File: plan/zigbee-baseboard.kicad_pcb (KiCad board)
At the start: 4 copper layers, 15.3 x 20.6 mm, 55 parts, among them J1 Debug_SWD_Pogo_2x3_P2.00mm, J2 EFR32MG24_Core_Expansion_L12, SW1 EVPBB2A9B000, U1 EFR32MG24B020F1536IM48-B, Y1 XTL501250-S315-038

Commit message: Adapt board size
The castellated pads currently doesn't really fit on the board.
The clearance to the lower board edge is not enough.
Therefore the board size has to get increased minimal to a size of 16x21mm
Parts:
- moved J2 0.40 mm to (133.8, 86.6)
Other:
- board size 15.3 x 20.6 mm -> 16 x 21 mm
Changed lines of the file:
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@@
 	)
 	(footprint "Smarthome:Module_EFR32MG24_Core_Castellated_L_12Pin_P2.54mm"
-		(locked yes)
 		(layer "F.Cu")
-		(at 134.2 86.64)
+		(at 133.8 86.64)
 		(property "Reference" "J2"
 			(at 5.5 0 0)
@@
 			(type default)
 		)
-		(layer "Edge.Cuts")
+		(layer "Dwgs.User")
 	)
 	(gr_line
@@
 			(type default)
 		)
-		(layer "Edge.Cuts")
+		(layer "Dwgs.User")
 	)
 	(gr_line
@@
 			(type default)
 		)
-		(layer "Edge.Cuts")
+		(layer "Dwgs.User")
 	)
 	(gr_line
@@
 			(type default)
 		)
+		(layer "Dwgs.User")
+	)
+	(gr_rect
+		(start 133.5 82)
+		(end 149.5 103)
+		(stroke
+			(width 0.05)
+			(type default)
+		)
+		(fill no)
 		(layer "Edge.Cuts")
 	)

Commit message: Place castellated pads on board edge
After adapting the board edges, place the castellated pads again on the board edge.
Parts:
- moved J2 0.50 mm to (133.5, 86.2)
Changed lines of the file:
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@@
 	)
 	(footprint "Smarthome:Module_EFR32MG24_Core_Castellated_L_12Pin_P2.54mm"
+		(locked yes)
 		(layer "F.Cu")
-		(at 133.8 86.64)
+		(at 133.5 86.24)
 		(property "Reference" "J2"
 			(at 5.5 0 0)

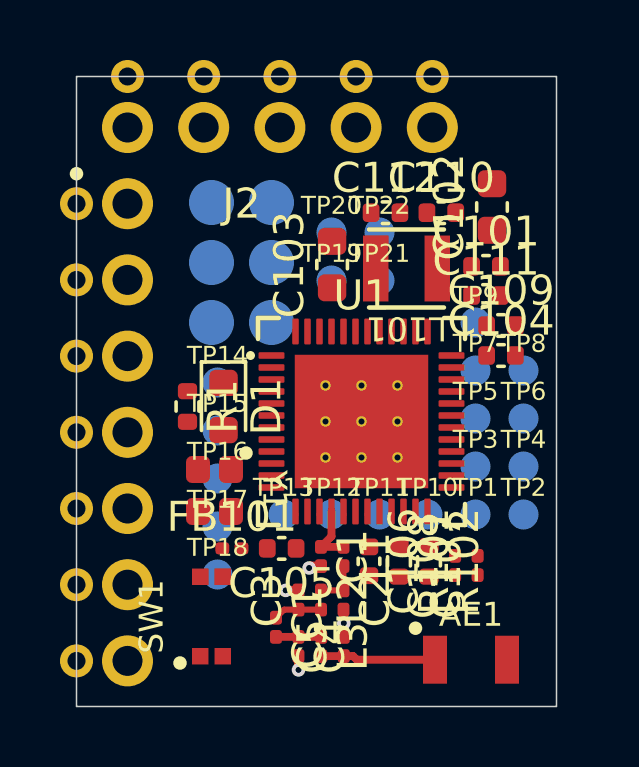
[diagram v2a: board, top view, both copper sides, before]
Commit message: Place GND area on F.Cu and In1.Cu
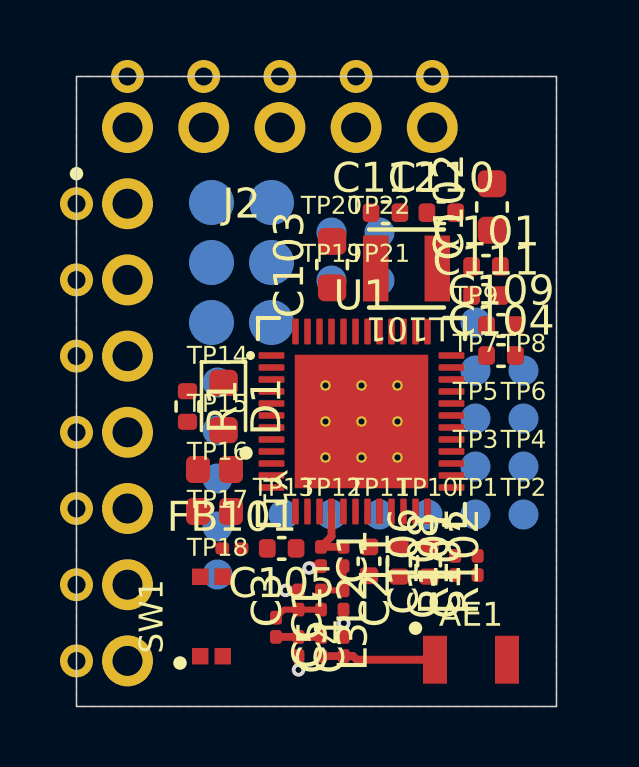
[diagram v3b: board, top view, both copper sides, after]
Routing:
- added copper zone on F.Cu, net GND
- added copper zone on In1.Cu, net GND
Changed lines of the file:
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@@
+	)
+	(zone
+		(net "GND")
+		(layer "F.Cu")
+		(hatch edge 0.5)
+		(priority 1)
+		(connect_pads yes
+			(clearance 0.2)
+		)
+		(min_thickness 0.2)
+		(fill yes
+			(thermal_gap 0.5)
+			(thermal_bridge_width 0.5)
+			(island_removal_mode 0)
+		)
+		(polygon
+			(pts
+				(xy 149.5 82) (xy 149.5 103) (xy 133.5 103) (xy 133.5 82)
+			)
+		)
 	)
 	(zone
@@
 			)
 		)
+	)
+	(zone
+		(net "GND")
+		(layer "In1.Cu")
+		(hatch edge 0.5)
+		(connect_pads yes
+			(clearance 0.2)
+		)
+		(min_thickness 0.2)
+		(fill yes
+			(thermal_gap 0.5)
+			(thermal_bridge_width 0.5)
+			(island_removal_mode 0)
+		)
+		(polygon
+			(pts
+				(xy 149.5 82) (xy 149.5 103) (xy 133.5 103) (xy 133.5 82)
+			)
+		)

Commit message: Route power lines
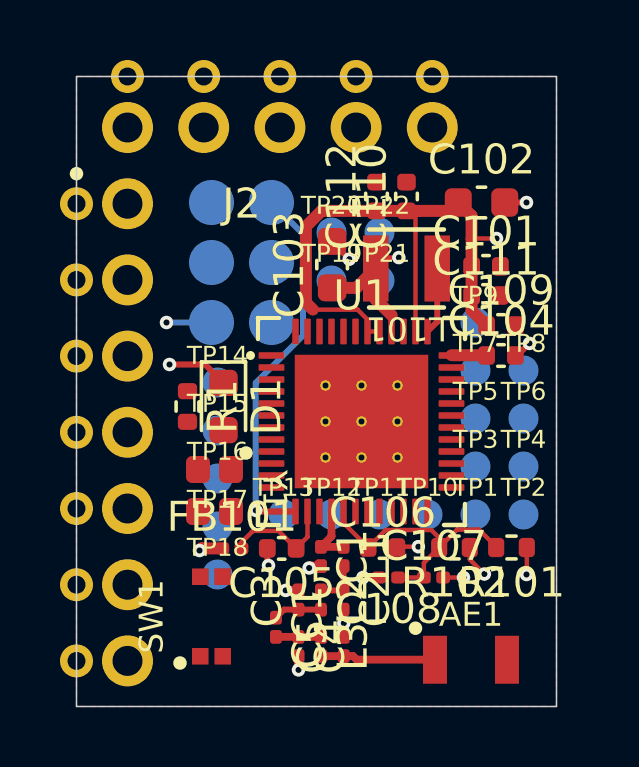
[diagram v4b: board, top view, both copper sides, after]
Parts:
- moved R101 3.78 mm to (148.0, 97.7), turned to 180 degrees
- moved C108 2.26 mm to (143.9, 98.7), turned to 180 degrees
- moved C107 1.52 mm to (145.4, 98.7), turned to 0 degrees
- moved C110 1.28 mm to (144.5, 86.0), turned to 90 degrees
- moved R102 0.97 mm to (146.1, 97.7), turned to 180 degrees
- moved C106 0.64 mm to (143.7, 97.7), turned to 0 degrees
- moved C112 0.62 mm to (143.5, 86.0), turned to 90 degrees
- moved C102 0.38 mm to (147.0, 86.2), turned to 0 degrees
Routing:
- net VBAT: track 0.00 -> 32.9 mm, vias 0 -> 2
- net VDCDC: track 0.00 -> 28.3 mm, vias 0 -> 3
- net ~{RESET}: track 0.00 -> 12.7 mm, vias 0 -> 1
- net PAVDD: track 0.00 -> 9.06 mm
- net GND: track 2.24 -> 10.6 mm, vias 4 -> 13
- net RFVDD: track 0.00 -> 3.81 mm
- net VREGSW: track 0.00 -> 2.23 mm
- net DECOUPLE: track 0.00 -> 1.17 mm

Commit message: Rout crystal and pogo pins
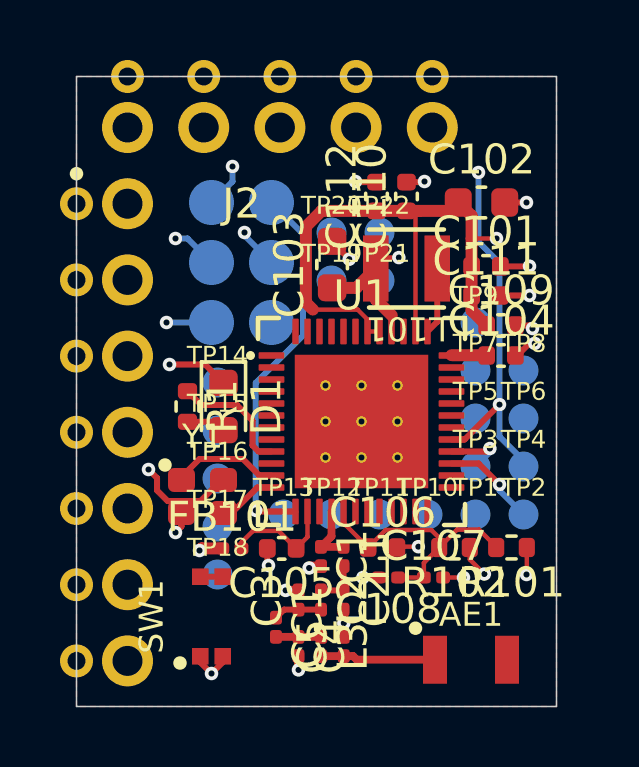
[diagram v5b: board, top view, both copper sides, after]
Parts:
- moved Y1 0.45 mm to (137.7, 96.0), turned to 0 degrees
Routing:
- net PA01: track 0.00 -> 23.3 mm, vias 0 -> 2
- net PA03: track 0.00 -> 22.3 mm, vias 0 -> 3
- net PA02: track 0.00 -> 17.1 mm, vias 0 -> 2
- net GND: track 10.6 -> 20.3 mm, vias 13 -> 21
- net PC08: track 0.00 -> 4.12 mm
- net Net-(U1-HFXTAL_I): track 0.00 -> 3.62 mm
- net Net-(U1-HFXTAL_O): track 0.00 -> 1.95 mm
- net Net-(D1-A): track 0.00 -> 1.31 mm
- net PC09: track 0.00 -> 0.75 mm

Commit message: Route pairing button and LED
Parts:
- moved D1 1.89 mm to (136.8, 92.0)
- moved R1 1.53 mm to (138.0, 91.7), turned to 90 degrees
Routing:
- net PC09: track 0.75 -> 9.09 mm, vias 0 -> 2
- net Net-(D1-A): track 1.31 -> 0.00 mm
- net GND: track 20.3 -> 19.4 mm, vias 21 -> 20
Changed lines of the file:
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@@
 	)
 	(footprint "LED_SMD:LED_0603_1608Metric"
-		(locked yes)
 		(layer "F.Cu")
-		(at 138.4 93 -90)
+		(at 136.8 92 -90)
 		(descr "LED SMD 0603 (1608 Metric), square (rectangular) end terminal, IPC-7351 nominal, (Body size source: http://www.tortai-tech.com/upload/download/2011102023233369053.pdf)")
 		(tags "LED")
@@
 	)
 	(footprint "Resistor_SMD:R_0402_1005Metric"
-		(locked yes)
 		(layer "F.Cu")
-		(at 137.2 93 -90)
+		(at 138 91.7 90)
 		(descr "Resistor SMD 0402 (1005 Metric), square (rectangular) end terminal, IPC-7351 nominal, (Body size source: IPC-SM-782 page 72, https://www.pcb-3d.com/wordpress/wp-content/uploads/ipc-sm-782a_amendment_1_and_2.pdf)")
 		(tags "resistor")
@@
 		(duplicate_pad_numbers_are_jumpers no)
 		(fp_line
-			(start -0.153641 0.38)
-			(end 0.153641 0.38)
+			(start -0.153641 -0.38)
+			(end 0.153641 -0.38)
 			(stroke
 				(width 0.12)
@@
 		)
 		(fp_line
-			(start -0.153641 -0.38)
-			(end 0.153641 -0.38)
+			(start -0.153641 0.38)
+			(end 0.153641 0.38)
 			(stroke
 				(width 0.12)
@@
 		)
 		(pad "1" smd roundrect
-			(at -0.51 0 270)
+			(at -0.51 0 90)
 			(size 0.54 0.64)
 			(layers "F.Cu" "F.Mask" "F.Paste")
@@
 		)
 		(pad "2" smd roundrect
-			(at 0.51 0 270)
+			(at 0.51 0 90)
 			(size 0.54 0.64)
 			(layers "F.Cu" "F.Mask" "F.Paste")
@@
 	)
 	(segment
-		(start 137.7875 91.6)
-		(end 136.6 91.6)
-		(width 0.2)
-		(layer "F.Cu")
-		(net "GND")
-	)
-	(segment
 		(start 142.02 87.517221)
 		(end 142.592172 88.089393)
@@
 	)
 	(segment
+		(start 136.8 91.2)
+		(end 136.5 90.9)
+		(width 0.15)
+		(layer "F.Cu")
+		(net "GND")
+	)
+	(segment
 		(start 147.775 86.2)
 		(end 148.5 86.2)
@@
 	)
 	(segment
-		(start 138.4 92.2125)
-		(end 137.7875 91.6)
-		(width 0.2)
+		(start 144.206893 97.673107)
+		(end 144.18 97.7)
+		(width 0.15)
 		(layer "F.Cu")
 		(net "GND")
 	)
 	(segment
-		(start 144.206893 97.673107)
-		(end 144.18 97.7)
+		(start 136.5 90.9)
+		(end 136.5 90.2)
 		(width 0.15)
 		(layer "F.Cu")
@@
 	)
 	(segment
+		(start 136.8 91.2125)
+		(end 136.8 91.2)
+		(width 0.15)
+		(layer "F.Cu")
+		(net "GND")
+	)
+	(segment
 		(start 138.337352 95.45)
 		(end 137.637352 96.15)
@@
 	)
 	(via
-		(at 136.6 91.6)
-		(size 0.45)
-		(drill 0.2)
-		(layers "F.Cu" "B.Cu")
-		(net "GND")
-	)
-	(via
 		(at 148.775 90.897025)
 		(size 0.45)
@@
 	)
 	(segment
-		(start 139.366487 93.470915)
-		(end 139.366487 94.296486)
-		(width 0.2)
+		(start 139.61674 94.5)
+		(end 139.15674 94.04)
+		(width 0.15)
 		(layer "F.Cu")
 		(net "PC08")
 	)
 	(segment
-		(start 138.845572 92.95)
-		(end 139.366487 93.470915)
-		(width 0.2)
+		(start 138 93.7)
+		(end 138 92.21)
+		(width 0.15)
 		(layer "F.Cu")
 		(net "PC08")
 	)
 	(segment
-		(start 139.570001 94.5)
-		(end 140 94.5)
-		(width 0.2)
+		(start 140 94.5)
+		(end 139.61674 94.5)
+		(width 0.15)
 		(layer "F.Cu")
 		(net "PC08")
 	)
 	(segment
-		(start 139.366487 94.296486)
-		(end 139.570001 94.5)
-		(width 0.2)
+		(start 138.34 94.04)
+		(end 138 93.7)
+		(width 0.15)
 		(layer "F.Cu")
 		(net "PC08")
 	)
 	(segment
-		(start 137.2 92.49)
-		(end 137.66 92.95)
-		(width 0.2)
+		(start 139.15674 94.04)
+		(end 138.34 94.04)
+		(width 0.15)
 		(layer "F.Cu")
 		(net "PC08")
 	)
 	(segment
-		(start 137.66 92.95)
-		(end 138.845572 92.95)
-		(width 0.2)
+		(start 139.55005 94.9)
+		(end 140 94.9)
+		(width 0.15)
 		(layer "F.Cu")
-		(net "PC08")
+		(net "PC09")
+	)
+	(segment
+		(start 137.031462 94.37)
+		(end 139.02005 94.37)
+		(width 0.15)
+		(layer "F.Cu")
+		(net "PC09")
+	)
+	(segment
+		(start 137.625 98.675)
+		(end 137.275 98.675)
+		(width 0.15)
+		(layer "F.Cu")
+		(net "PC09")
+	)
+	(segment
+		(start 139.02005 94.37)
+		(end 139.55005 94.9)
+		(width 0.15)
+		(layer "F.Cu")
+		(net "PC09")
 	)
 	(segment
@@
 	)
 	(segment
-		(start 137.6 94.75)
-		(end 139.045572 94.75)
+		(start 137.275 98.675)
+		(end 136.8 98.2)
+		(width 0.15)
+		(layer "F.Cu")
+		(net "PC09")
+	)
+	(via
+		(at 136.8 98.2)
+		(size 0.45)
+		(drill 0.2)
+		(layers "F.Cu" "B.Cu")
+		(net "PC09")
+	)
+	(via
+		(at 137.031462 94.37)
+		(size 0.45)
+		(drill 0.2)
+		(layers "F.Cu" "B.Cu")
+		(net "PC09")
+	)
+	(segment
+		(start 137.031462 94.37)
+		(end 137.031462 94.73)
+		(width 0.15)
+		(layer "In2.Cu")
+		(net "PC09")
+	)
+	(segment
+		(start 137.28 97.398823)
+		(end 136.8 97.878823)
+		(width 0.15)
+		(layer "In2.Cu")
+		(net "PC09")
+	)
+	(segment
+		(start 137.28 94.978538)
+		(end 137.28 97.398823)
+		(width 0.15)
+		(layer "In2.Cu")
+		(net "PC09")
+	)
+	(segment
+		(start 136.8 97.878823)
+		(end 136.8 98.2)
+		(width 0.15)
+		(layer "In2.Cu")
+		(net "PC09")
+	)
+	(segment
+		(start 137.031462 94.73)
+		(end 137.28 94.978538)
+		(width 0.15)
+		(layer "In2.Cu")
+		(net "PC09")
+	)
+	(segment
+		(start 138.862648 94.75)
+		(end 137.6 94.75)
 		(width 0.2)
 		(layer "F.Cu")
@@
 	)
 	(segment
-		(start 139.045572 94.75)
-		(end 139.595572 95.3)
+		(start 140 95.3)
+		(end 139.412648 95.3)
 		(width 0.2)
 		(layer "F.Cu")
@@
 	)
 	(segment
-		(start 139.595572 95.3)
-		(end 140 95.3)
+		(start 139.412648 95.3)
+		(end 138.862648 94.75)
 		(width 0.2)
 		(layer "F.Cu")
@@
 		(net "Net-(C2-Pad1)")
 	)
-	(segment
-		(start 137.2 93.51)
-		(end 138.1225 93.51)
-		(width 0.2)
-		(layer "F.Cu")
-		(net "Net-(D1-A)")
-	)
-	(segment
-		(start 138.1225 93.51)
-		(end 138.4 93.7875)
-		(width 0.2)
-		(layer "F.Cu")
-		(net "Net-(D1-A)")
-	)
 	(zone
